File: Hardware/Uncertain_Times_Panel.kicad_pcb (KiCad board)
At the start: 2 copper layers, 71 x 128.5 mm, 21 parts

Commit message: Reduced Panel Size
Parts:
- removed the Ref** at (94.0, 141.0)
- removed the Ref** at (115.0, 141.0)
- removed the Ref** at (104.5, 141.0)
- added Ref**: Thonkiconn_Socket_MountingHole_6mm, Custom_Footprints:Thonkiconn_Socket_MountingHole_6mm, F.Cu at (98.0, 126.0)
- added Ref**: Thonkiconn_Socket_MountingHole_6mm, Custom_Footprints:Thonkiconn_Socket_MountingHole_6mm, F.Cu at (98.0, 139.0)
- added Ref**: Thonkiconn_Socket_MountingHole_6mm, Custom_Footprints:Thonkiconn_Socket_MountingHole_6mm, F.Cu at (86.0, 139.0)
- moved Ref** 20.2 mm to (74.0, 139.0)
- moved Ref** 15.5 mm to (68.0, 126.0)
- moved Ref** 15.1 mm to (80.0, 126.0)
- moved Ref** 11.7 mm to (62.0, 139.0)
- moved Ref** 10.2 mm to (108.3, 155.5)
- moved Ref** 10.1 mm to (108.4, 33.0)
- moved Ref** 4.00 mm to (105.0, 95.5)
- moved Ref** 4.00 mm to (105.0, 51.0)
- moved Ref** 4.00 mm to (105.0, 71.0)
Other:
- board size 71 x 128.5 mm -> 60.8 x 128.5 mm
- board text added: "FM Out"
- board text added: "Ramp"
- board text added: "Sine Out"
- board text added: "Swell"
- board text removed: "A OUT B"
- board text removed: "PITCH"
- board text removed: "VCA"
- board text removed: "WARP"

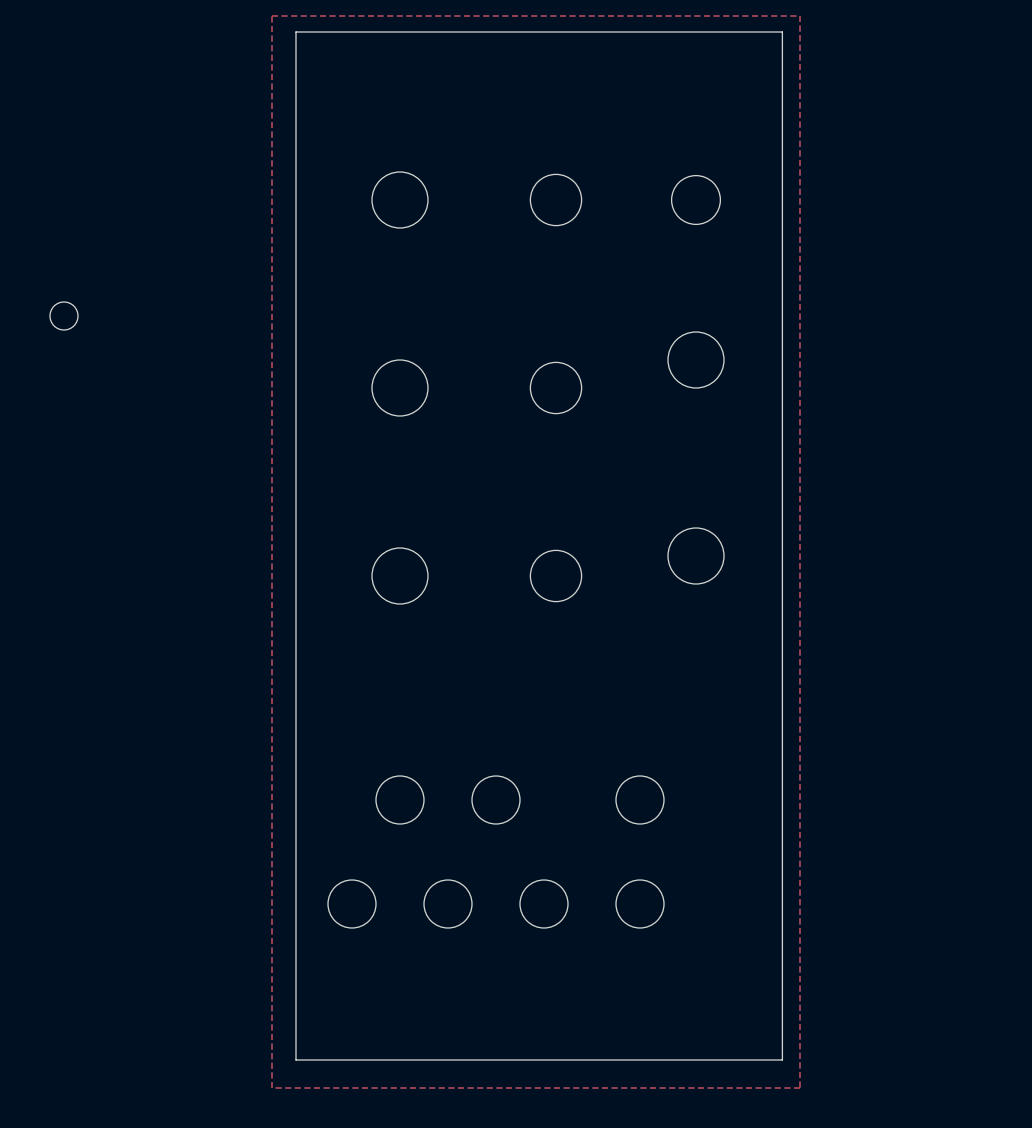
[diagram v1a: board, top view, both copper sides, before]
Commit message: More panel layout
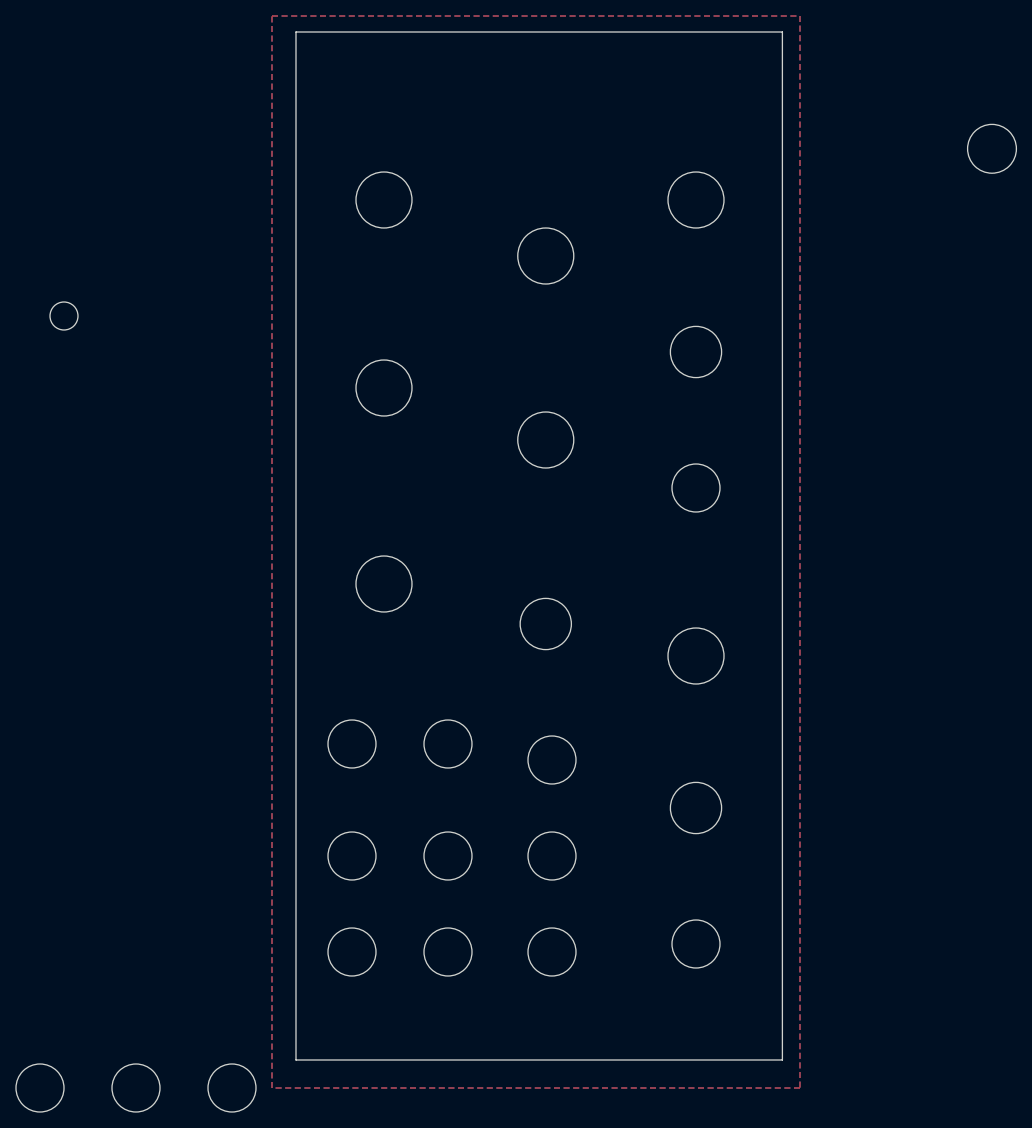
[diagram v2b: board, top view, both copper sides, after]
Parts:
- removed the Ref** at (87.5, 74.5)
- removed the Ref** at (98.0, 139.0)
- removed the Ref** at (105.0, 95.5)
- removed the Ref** at (87.5, 51.0)
- added Ref**: Alpha_9mm_pot_hole, Custom_Footprints:Alpha_9mm_pot_hole, F.Cu at (105.0, 108.0)
- added Ref**: Thonkiconn_Socket_MountingHole_6mm, Custom_Footprints:Thonkiconn_Socket_MountingHole_6mm, F.Cu at (74.0, 119.0)
- added Ref**: Tall_Trimmer_Hole, Custom_Footprints:Tall_Trimmer_Hole, F.Cu at (105.0, 127.0)
- added Ref**: Thonkiconn_Socket_MountingHole_6mm, Custom_Footprints:Thonkiconn_Socket_MountingHole_6mm, F.Cu at (62.0, 119.0)
- added Ref**: Thonkiconn_Socket_MountingHole_6mm, Custom_Footprints:Thonkiconn_Socket_MountingHole_6mm, F.Cu at (87.0, 145.0)
- added Ref**: Thonkiconn_Socket_MountingHole_6mm, Custom_Footprints:Thonkiconn_Socket_MountingHole_6mm, F.Cu at (74.0, 133.0)
- added Ref**: Tall_Trimmer_Hole, Custom_Footprints:Tall_Trimmer_Hole, F.Cu at (105.0, 70.0)
- added Ref**: Thonkiconn_Socket_MountingHole_6mm, Custom_Footprints:Thonkiconn_Socket_MountingHole_6mm, F.Cu at (105.0, 144.0)
- added Ref**: Alpha_9mm_pot_hole, Custom_Footprints:Alpha_9mm_pot_hole, F.Cu at (86.2, 58.0)
- added Ref**: Thonkiconn_Socket_MountingHole_6mm, Custom_Footprints:Thonkiconn_Socket_MountingHole_6mm, F.Cu at (62.0, 133.0)
- added Ref**: Thonkiconn_Socket_MountingHole_6mm, Custom_Footprints:Thonkiconn_Socket_MountingHole_6mm, F.Cu at (62.0, 145.0)
- added Ref**: Alpha_9mm_pot_hole, Custom_Footprints:Alpha_9mm_pot_hole, F.Cu at (86.2, 81.0)
- added Ref**: Thonkiconn_Socket_MountingHole_6mm, Custom_Footprints:Thonkiconn_Socket_MountingHole_6mm, F.Cu at (74.0, 145.0)
- moved Ref** 45.3 mm to (35.0, 162.0)
- moved Ref** 45.3 mm to (47.0, 162.0)
- moved Ref** 45.3 mm to (23.0, 162.0)
- moved Ref** 39.6 mm to (105.0, 87.0)
- moved Ref** 37.5 mm to (142.0, 44.6)
- moved Ref** 20.2 mm to (87.0, 133.0)
- moved Ref** 20.0 mm to (105.0, 51.0)
- moved Ref** 8.60 mm to (87.0, 121.0)
- moved Ref** 6.13 mm to (86.2, 104.0)
- moved Ref** 2.24 mm to (66.0, 99.0)
- moved Ref** 2.00 mm to (66.0, 51.0)
- moved Ref** 2.00 mm to (66.0, 74.5)
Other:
- board text added: "1"
- board text added: "2"
- board text added: "3"
- board text added: "CLK"
- board text added: "FM"
- board text added: "GATE"
- board text removed: "Time"

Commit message: First draft panel layout
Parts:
- removed the Ref** at (74.0, 119.0)
- removed the Ref** at (62.0, 119.0)
- removed the Ref** at (86.2, 104.0)
- added Ref**: Alpha_9mm_pot_hole, Custom_Footprints:Alpha_9mm_pot_hole, F.Cu at (86.0, 108.0)
- moved Ref** 56.1 mm to (109.0, 143.0)
- moved Ref** 33.3 mm to (62.0, 143.0), turned to 90 degrees
- moved Ref** 29.3 mm to (103.0, 129.0)
- moved Ref** 19.4 mm to (73.0, 129.0)
- moved Ref** 19.0 mm to (105.0, 89.0)
- moved Ref** 19.0 mm to (105.0, 108.0)
- moved Ref** 18.9 mm to (84.0, 129.0)
- moved Ref** 17.2 mm to (73.0, 143.0), turned to 90 degrees
- moved Ref** 7.07 mm to (98.0, 143.0)
- moved Ref** 4.00 mm to (62.0, 129.0)
- moved Ref** 3.61 mm to (84.0, 143.0), turned to 90 degrees
- moved Ref** 2.01 mm to (86.0, 83.0)
- moved Ref** 2.00 mm to (66.0, 101.0)
- moved Ref** 1.50 mm to (66.0, 76.0)
- moved Ref** 0.22 mm to (86.0, 58.0)

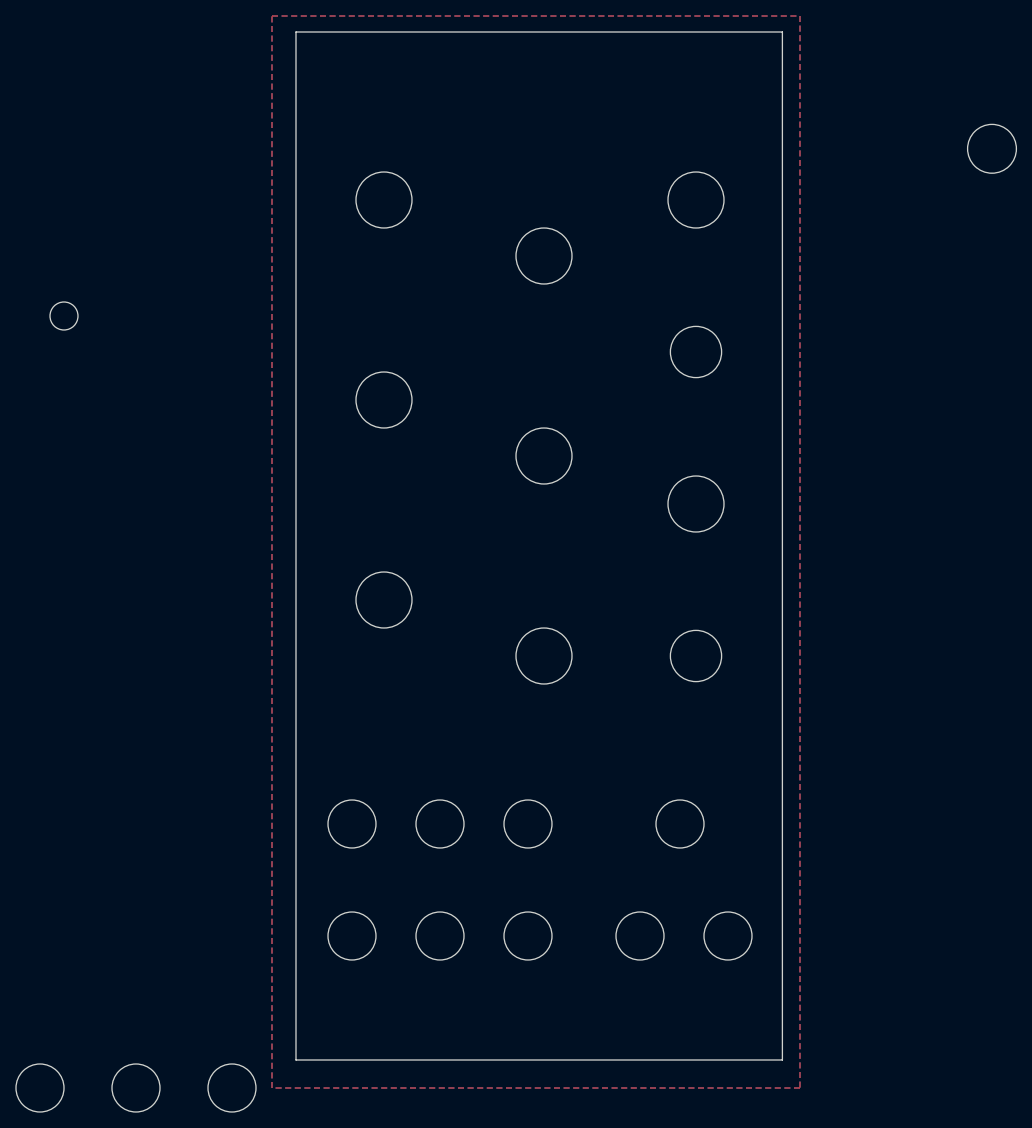
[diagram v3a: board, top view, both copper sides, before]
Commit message: Started to prepare Component schematic
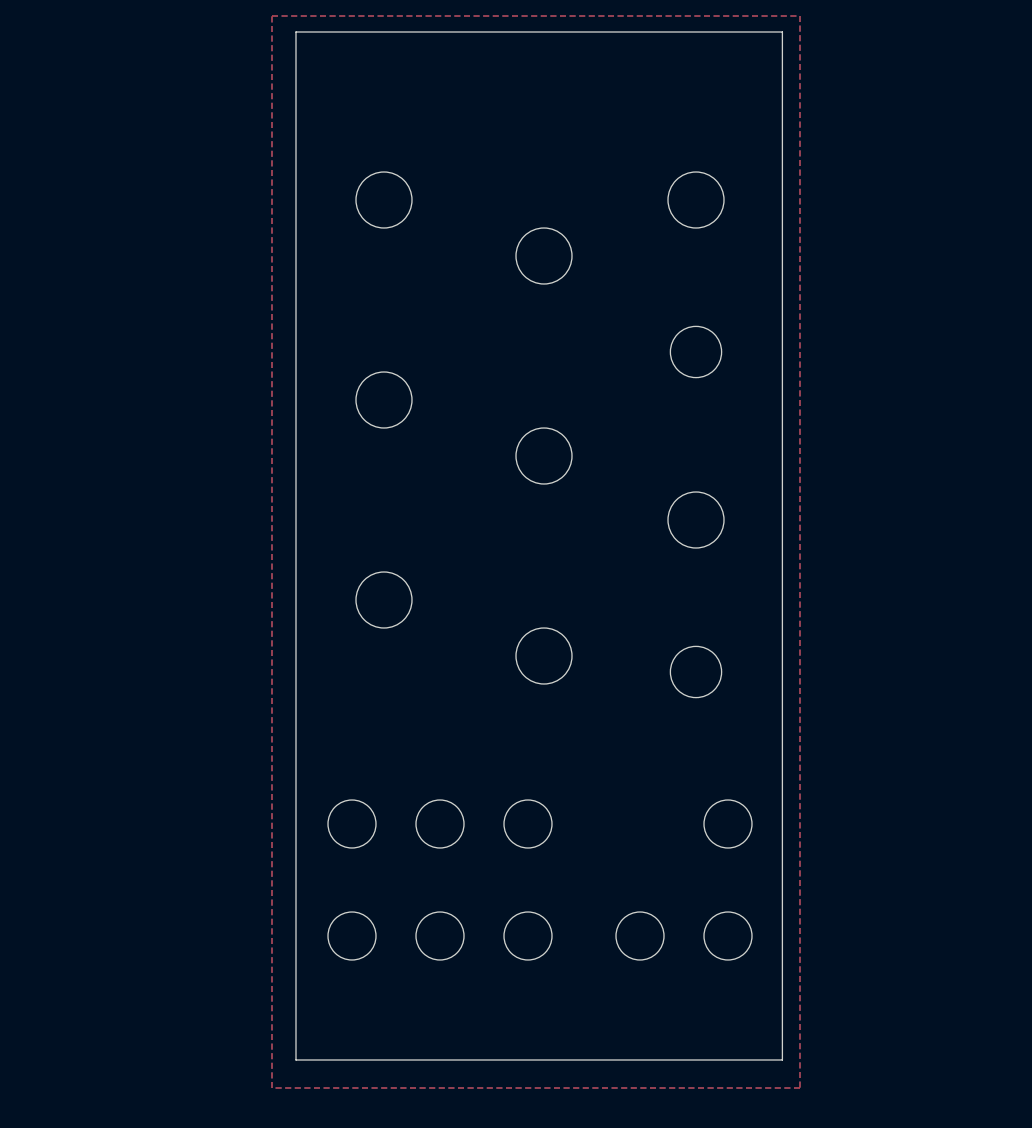
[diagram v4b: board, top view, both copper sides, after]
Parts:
- removed the Ref** at (47.0, 162.0)
- removed the Ref** at (35.0, 162.0)
- removed the Ref** at (23.0, 162.0)
- removed the Ref** at (142.0, 44.6)
- removed the Ref** at (26.0, 65.5)
- moved Ref** 6.00 mm to (109.0, 129.0), turned to 180 degrees
- moved Ref** 2.00 mm to (105.0, 91.0)
- moved Ref** 2.00 mm to (105.0, 110.0), turned to 0 degrees
- turned Ref** to 180 degrees (x8)
- turned Ref** to 0 degrees
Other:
- board text removed: "FM Out"
- board text removed: "Oct"
- board text removed: "Sine Out"

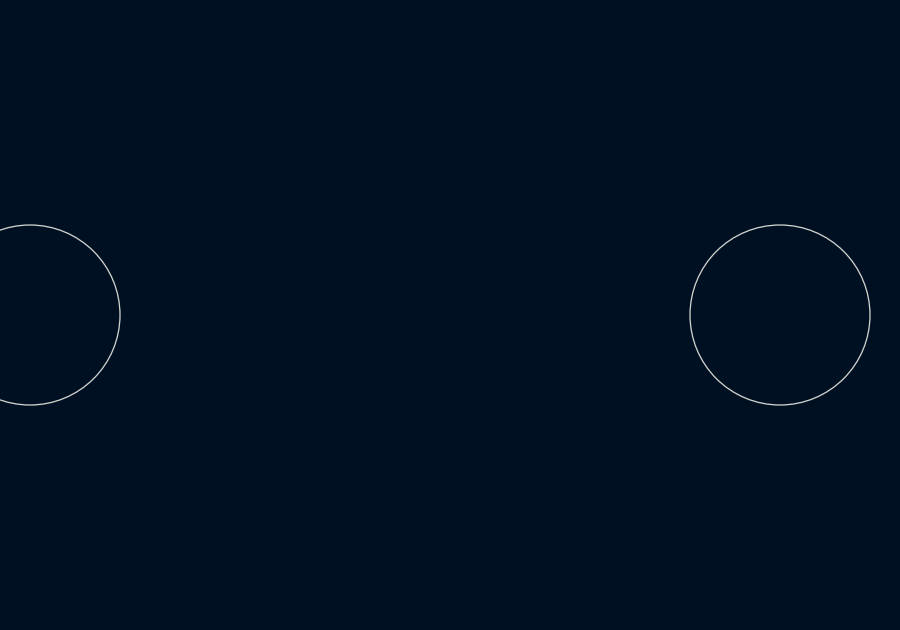
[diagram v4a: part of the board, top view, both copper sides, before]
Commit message: Added logo and LEDs to panel
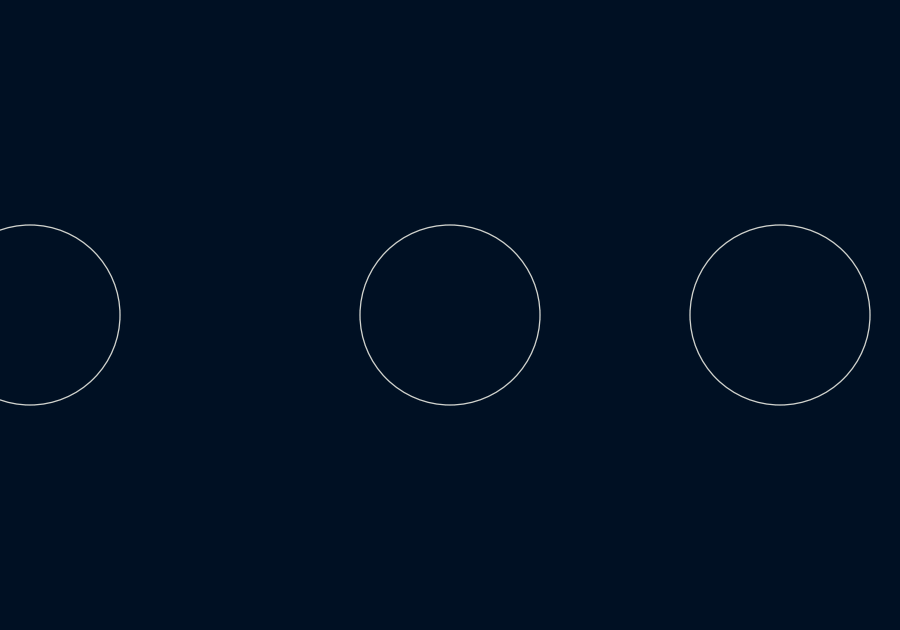
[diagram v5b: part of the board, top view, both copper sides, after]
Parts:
- added G***: LOGO, Graphics:SinosaurLogo, F.Cu at (84.3, 34.3)
- added Ref**: Thonkiconn_Socket_MountingHole_6mm, Custom_Footprints:Thonkiconn_Socket_MountingHole_6mm, F.Cu at (98.0, 129.0)
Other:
- board text added: "Sine"
- board text added: "Ø"

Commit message: First draft of schematic
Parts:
- added kibuzzard-666C296D: G***, kibuzzard-666C296D, F.Cu at (62.0, 136.0)
- added kibuzzard-666C29A3: G***, kibuzzard-666C29A3, F.Cu at (73.0, 136.0)
- added kibuzzard-666C29AC: G***, kibuzzard-666C29AC, F.Cu at (84.0, 136.0)
- added kibuzzard-666C2AB0: G***, kibuzzard-666C2AB0, F.Cu at (57.0, 51.0)
- added kibuzzard-666C2AB5: G***, kibuzzard-666C2AB5, F.Cu at (57.0, 76.0)
- added kibuzzard-666C2ABA: G***, kibuzzard-666C2ABA, F.Cu at (57.0, 101.0)
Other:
- board text added: "Rate"
- board text removed: "2"
- board text removed: "3"
- board text removed: "Speed"
